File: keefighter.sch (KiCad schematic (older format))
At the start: 49 parts, among them SW0 SW_PUSH, SW1 SW_PUSH, SW10 SW_PUSH, SW11 SW_PUSH, SW12 SW_PUSH, SW13 SW_PUSH, SW14 SW_PUSH, SW15 SW_PUSH, SW16 SW_PUSH, SW17 SW_PUSH, SW2 SW_PUSH, SW3 SW_PUSH, SW4 SW_PUSH, SW5 SW_PUSH, SW6 SW_PUSH, SW7 SW_PUSH, SW8 SW_PUSH, SW9 SW_PUSH, U1 ProMicro

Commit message: Initial Commit
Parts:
- removed D0, D1, D10, D11, D12, D13, D14, D15, D16, D17, D2, D3, D4, D5, D6, D7, D8, D9: 1N4148, Diode_THT:D_DO-35_SOD27_P7.62mm_Horizontal, symbol Diode:1N4148
- removed LED0, LED1, LED10, LED11, LED2, LED3, LED4, LED5, LED6, LED7, LED8, LED9: SK6812MINI, kbd:YS-SK6812MINI-E, symbol keefighter-rescue:SK6812MINI-kbd
- removed SW0, SW12, SW15, SW3, SW6, SW9: SW_PUSH, Button_Switch_THT:SW_PUSH_6mm, symbol keefighter-rescue:SW_PUSH-kbd
- removed SW1, SW10, SW11, SW13, SW14, SW16, SW17, SW2, SW4, SW5, SW7, SW8: SW_PUSH, kbd:CherryMX_Hotswap, symbol keefighter-rescue:SW_PUSH-kbd
- removed U1: ProMicro, pro micro:SPARKFUN_PRO_MICRO, symbol keefighter-rescue:ProMicro-kbd
- added C0, C1, C2, C3: 0.1u, symbol Device:C_Small
- added C4: 10u, symbol Device:C_Small
- added C5, C6: 22p, symbol Device:C_Small
- added C7: 1u, symbol Device:C_Small
- added D0, D1, D10, D11, D12, D13, D14, D15, D16, D17, D18, D19, D2, D20, D21, D22, D23, D24, D25, D26, D27, D28, D29, D3, D30, D31, D32, D33, D34, D4, D5, D6, D7, D8, D9: D, symbol Device:D
- added D35: PRTR5V0U2X, Package_TO_SOT_SMD:SOT-143, symbol Power_Protection:PRTR5V0U2X
- added F0: 500m, symbol Device:Polyfuse_Small
- added J0: AVR-ISP-6, symbol Connector:AVR-ISP-6
- added R0, R1: 10k, symbol Device:R_Small
- added R2, R3: 22, symbol Device:R_Small
- added R4, R5: 5.1k, symbol Device:R_Small
- added SW0, SW1, SW10, SW11, SW12, SW13, SW14, SW15, SW16, SW17, SW18, SW19, SW2, SW20, SW21, SW22, SW23, SW24, SW25, SW26, SW27, SW28, SW29, SW3, SW30, SW31, SW32, SW33, SW34, SW4, SW5, SW6, SW7, SW8, SW9: SW_Push, symbol Switch:SW_Push
- added SW35: SW_Push_Reset, symbol Switch:SW_Push
- added U0: ATmega32U4-AU, Package_QFP:TQFP-44_10x10mm_P0.8mm, symbol MCU_Microchip_ATmega:ATmega32U4-AU
- added USB0: HRO-TYPE-C-31-M-12, symbol Type-C:HRO-TYPE-C-31-M-12
- added X0: XTAL, symbol Device:Crystal_GND24_Small
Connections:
- net labels added: +5V, D+, D-, GND, MISO, MOSI, RESET, SCK, VCC, XTAL1, XTAL2, col10, col11, col12, col6, col7, col8, col9
- net labels removed: din, gnd, vcc
- wire segments 115 -> 180
- no-connect marks 0 -> 10

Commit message: asdfasf
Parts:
- removed SW1, SW33: SW_Push, symbol Switch:SW_Push
- added JOY0, JOY1: COM-09032, XDCR_COM-09032, symbol Joystick:COM-09032
- C0, C1, C2, C3, C4, C5, C6, C7: footprint (none) -> Capacitor_SMD:C_0805_2012Metric_Pad1.18x1.45mm_HandSolder
- D0, D1, D10, D11, D12, D13, D14, D15, D16, D17, D18, D19, D2, D20, D21, D22, D23, D24, D25, D26, D27, D28, D29, D3, D30, D31, D32, D33, D34, D4, D5, D6, D7, D8, D9: footprint (none) -> lib:D3_TH_SMD_v2
- D35: footprint Package_TO_SOT_SMD:SOT-143 -> lib:SOT143B
- F0: footprint (none) -> Fuse:Fuse_1206_3216Metric_Pad1.42x1.75mm_HandSolder
- J0: footprint (none) -> lib:Reset_Pretty-Mask
- R0, R1, R2, R3, R4, R5: footprint (none) -> Resistor_SMD:R_0805_2012Metric_Pad1.20x1.40mm_HandSolder
- USB0: footprint (none) -> lib:HRO-TYPE-C-31-M-12-HandSoldering
- X0: footprint (none) -> Crystal:Crystal_SMD_3225-4Pin_3.2x2.5mm_HandSoldering
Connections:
- net col1: now also JOY0.B1A (SEL+), JOY1.B1A (SEL+)
- net at D1.2 (A): now also JOY0.B2A (SEL-)
- net at D33.2 (A): now also JOY1.B2A (SEL-)
- new net: JOY0.S1 (SHIELD), JOY0.S2 (SHIELD), JOY0.S3 (SHIELD), JOY0.S4 (SHIELD)
- new net: JOY1.S1 (SHIELD), JOY1.S2 (SHIELD), JOY1.S3 (SHIELD), JOY1.S4 (SHIELD)
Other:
- moved on the sheet: C0, C1, C2, C3, C4, C5, C6, C7, D0, D1, D10, D11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

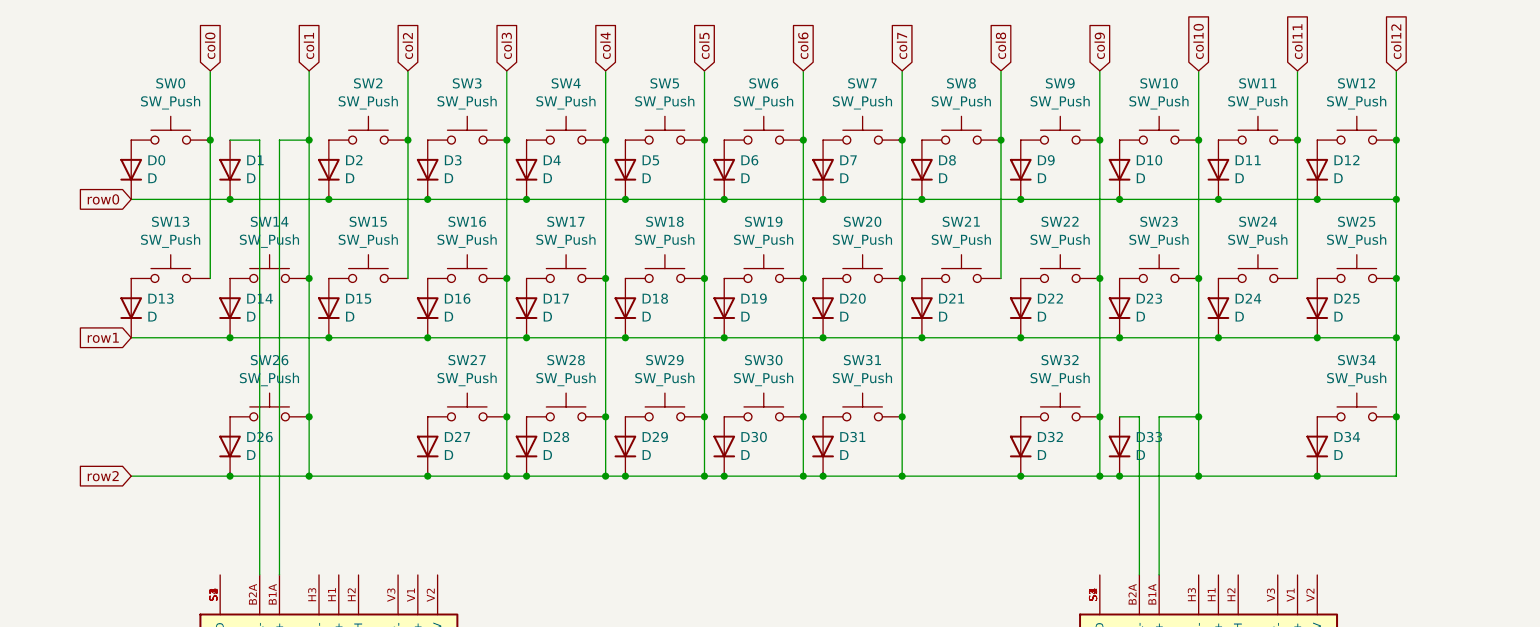
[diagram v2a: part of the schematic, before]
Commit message: Fixed routing issues with matrix
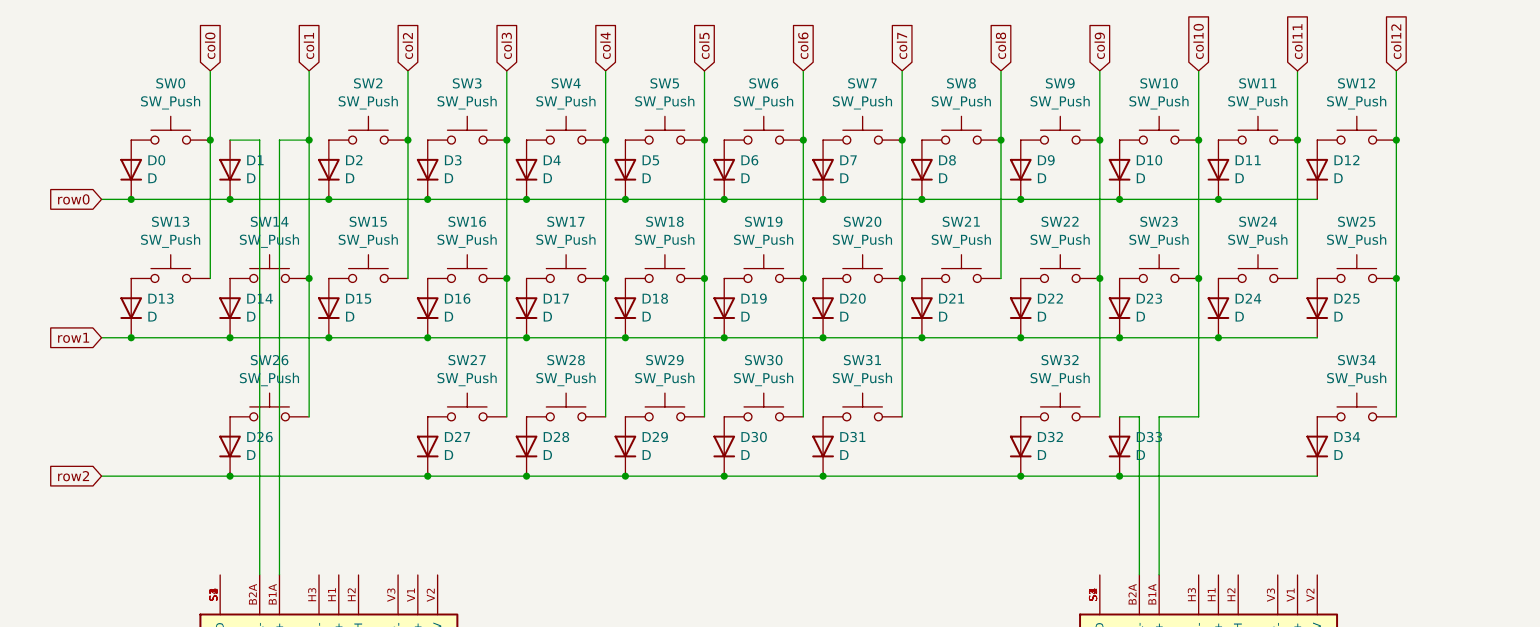
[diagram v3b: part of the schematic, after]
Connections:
- net col1: no longer D0.1 (K), D1.1 (K), D10.1 (K), D11.1 (K), D12.1 (K), D13.1 (K), D14.1 (K), D15.1 (K), D16.1 (K), D17.1 (K), D18.1 (K), D19.1 (K), D2.1 (K), D20.1 (K), D21.1 (K), D22.1 (K), D23.1 (K), D24.1 (K), D25.1 (K), D26.1 (K), D27.1 (K), D28.1 (K), D29.1 (K), D3.1 (K), D30.1 (K), D31.1 (K), D32.1 (K), D33.1 (K), D34.1 (K), D4.1 (K), D5.1 (K), D6.1 (K), D7.1 (K), D8.1 (K), D9.1 (K), JOY1.B1A (SEL+), SW10.2, SW12.2, SW16.2, SW17.2, SW18.2, SW19.2, SW20.2, SW22.2, SW23.2, SW25.2, SW27.2, SW28.2, SW29.2, SW3.2, SW30.2, SW31.2, SW32.2, SW34.2, SW4.2, SW5.2, SW6.2, SW7.2, SW9.2, U0.1 (PE6), U0.18 (PD0), U0.19 (PD1), U0.20 (PD2), U0.21 (PD3), U0.22 (PD5), U0.26 (PD6), U0.28 (PB4), U0.29 (PB5), U0.32 (PC7), U0.8 (PB0)
- new net col10: JOY1.B1A (SEL+), SW10.2, SW23.2, U0.26 (PD6)
- new net col12: SW12.2, SW25.2, SW34.2, U0.1 (PE6)
- new net col3: SW16.2, SW27.2, SW3.2, U0.32 (PC7)
- new net col4: SW17.2, SW28.2, SW4.2, U0.18 (PD0)
- new net col5: SW18.2, SW29.2, SW5.2, U0.19 (PD1)
- new net col6: SW19.2, SW30.2, SW6.2, U0.20 (PD2)
- new net col7: SW20.2, SW31.2, SW7.2, U0.21 (PD3)
- new net col9: SW22.2, SW32.2, SW9.2, U0.22 (PD5)
- new net row0: D0.1 (K), D1.1 (K), D10.1 (K), D11.1 (K), D12.1 (K), D2.1 (K), D3.1 (K), D4.1 (K), D5.1 (K), D6.1 (K), D7.1 (K), D8.1 (K), D9.1 (K), U0.8 (PB0)
- new net row1: D13.1 (K), D14.1 (K), D15.1 (K), D16.1 (K), D17.1 (K), D18.1 (K), D19.1 (K), D20.1 (K), D21.1 (K), D22.1 (K), D23.1 (K), D24.1 (K), D25.1 (K), U0.28 (PB4)
- new net row2: D26.1 (K), D27.1 (K), D28.1 (K), D29.1 (K), D30.1 (K), D31.1 (K), D32.1 (K), D33.1 (K), D34.1 (K), U0.29 (PB5)
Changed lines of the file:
@@
 Text GLabel 10600 1450 2    50   Input ~ 0
 MISO
-Wire Wire Line
-	5550 2900 5950 2900
 $Comp
 L Device:D D32
@@
 	1    0    0    -1
 $EndComp
-Wire Wire Line
-	4550 2900 4950 2900
 $Comp
 L Device:D D31
@@
 	1    0    0    -1
 $EndComp
-Wire Wire Line
-	4050 2900 4450 2900
 $Comp
 L Device:D D30
@@
 	1    0    0    -1
 $EndComp
-Wire Wire Line
-	3550 2900 3950 2900
 $Comp
 L Device:D D29
@@
 	1    0    0    -1
 $EndComp
-Wire Wire Line
-	3050 2900 3450 2900
 $Comp
 L Device:D D28
@@
 	1    0    0    -1
 $EndComp
-Wire Wire Line
-	2550 2900 2950 2900
 $Comp
 L Device:D D27
@@
 	1    0    0    -1
 $EndComp
-Connection ~ 1950 2600
-Wire Wire Line
-	1550 2900 1950 2900
 $Comp
 L Device:D D26
@@
 $EndComp
 Wire Wire Line
-	2450 850  2450 1200
-Wire Wire Line
 	2050 1500 2550 1500
 $Comp
@@
 	0    -1   -1   0
 $EndComp
-Wire Wire Line
-	1950 2600 1950 2900
-Wire Wire Line
-	2950 2600 2950 2900
-Connection ~ 2950 2900
-Wire Wire Line
-	2950 2900 3050 2900
-Wire Wire Line
-	3450 2600 3450 2900
-Connection ~ 3450 2900
-Wire Wire Line
-	3450 2900 3550 2900
-Wire Wire Line
-	3950 2600 3950 2900
-Connection ~ 3950 2900
-Wire Wire Line
-	3950 2900 4050 2900
-Wire Wire Line
-	4450 2600 4450 2900
-Connection ~ 4450 2900
-Wire Wire Line
-	4450 2900 4550 2900
-Wire Wire Line
-	4950 2600 4950 2900
-Wire Wire Line
-	5950 2600 5950 2900
-Wire Wire Line
-	5950 2900 6050 2900
 Connection ~ 4550 1500
 Connection ~ 4550 2200
@@
 Connection ~ 1450 1200
 Wire Wire Line
-	2450 1200 2450 1900
-Connection ~ 2450 1200
-Wire Wire Line
 	2950 1200 2950 1900
 Connection ~ 2950 1200
@@
 Connection ~ 3450 1200
 Wire Wire Line
-	3950 1200 3950 1900
-Connection ~ 3950 1200
-Wire Wire Line
-	4450 1200 4450 1900
-Connection ~ 4450 1200
-Wire Wire Line
 	4950 850  4950 1200
 Wire Wire Line
@@
 	6950 1900 6950 1200
 Wire Wire Line
-	7450 1900 7450 1500
-Wire Wire Line
 	5950 850  5950 1200
 Connection ~ 5950 1200
@@
 	7450 850  7450 1200
 Connection ~ 7450 1200
-Connection ~ 3050 2900
-Connection ~ 3550 2900
-Connection ~ 4050 2900
-Connection ~ 4550 2900
-Wire Wire Line
-	6050 2900 6450 2900
 $Comp
 L Device:D D33
@@
 	0    -1   -1   0
 $EndComp
-Wire Wire Line
-	7050 2900 7450 2900
 $Comp
 L Device:D D34
@@
 $EndComp
 Wire Wire Line
-	7450 2600 7450 2900
-Connection ~ 6050 2900
-Connection ~ 5950 2900
-Wire Wire Line
 	1950 1900 1950 2600
-Connection ~ 1950 1900
 Wire Wire Line
 	2950 1900 2950 2600
 Connection ~ 2950 1900
-Connection ~ 2950 2600
 Wire Wire Line
 	3450 1900 3450 2600
 Connection ~ 3450 1900
-Connection ~ 3450 2600
-Wire Wire Line
-	3950 1900 3950 2600
-Connection ~ 3950 1900
-Connection ~ 3950 2600
 Wire Wire Line
 	4450 1900 4450 2600
-Connection ~ 4450 1900
-Connection ~ 4450 2600
 Wire Wire Line
 	4950 1900 4950 2600
 Connection ~ 4950 1900
-Connection ~ 4950 2600
 Wire Wire Line
 	5950 1900 5950 2600
 Connection ~ 5950 1900
-Connection ~ 5950 2600
 Connection ~ 6450 1900
-Wire Wire Line
-	7450 1900 7450 2200
 Connection ~ 7450 1900
-Connection ~ 7450 2600
-Wire Wire Line
-	7050 1500 7450 1500
-Connection ~ 7050 1500
-Connection ~ 7450 1500
-Wire Wire Line
-	7450 1500 7450 1200
-Wire Wire Line
-	7050 2200 7450 2200
-Connection ~ 7050 2200
-Connection ~ 7450 2200
-Wire Wire Line
-	7450 2200 7450 2600
-Wire Wire Line
-	7050 2900 6450 2900
-Connection ~ 7050 2900
-Connection ~ 6450 2900
-Wire Wire Line
-	5550 2900 4950 2900
-Connection ~ 5550 2900
-Connection ~ 4950 2900
-Wire Wire Line
-	2550 2900 1950 2900
-Connection ~ 2550 2900
-Connection ~ 1950 2900
-Connection ~ 1550 2900
 Wire Wire Line
 	10350 1450 10600 1450
@@
 $EndComp
 Wire Wire Line
-	1950 850  1950 1200
-Connection ~ 1950 1200
-Wire Wire Line
-	1950 1200 1950 1900
-Wire Wire Line
 	1800 1200 1950 1200
 Wire Wire Line
@@
 Wire Wire Line
 	6150 2600 6050 2600
-Connection ~ 6450 2600
-Wire Wire Line
-	6450 2600 6450 2900
 Wire Wire Line
 	1550 1200 1700 1200
@@
 Text GLabel 10350 1750 2    50   Input ~ 0
 col0
-Wire Wire Line
-	1050 2900 1550 2900
-Text GLabel 1050 2900 0    50   Input ~ 0
+Text GLabel 900  2900 0    50   Input ~ 0
 row2
-Text GLabel 1050 2200 0    50   Input ~ 0
+Text GLabel 900  2200 0    50   Input ~ 0
 row1
-Text GLabel 1050 1500 0    50   Input ~ 0
+Text GLabel 900  1500 0    50   Input ~ 0
 row0
+Wire Wire Line
+	2450 1200 2450 1900
+Connection ~ 2450 1200
+Wire Wire Line
+	2450 850  2450 1200
+Connection ~ 1950 1900
+Wire Wire Line
+	1950 1200 1950 1900
+Connection ~ 1950 1200
+Wire Wire Line
+	1950 850  1950 1200
+Wire Wire Line
+	3950 1900 3950 2600
+Connection ~ 4450 1900
+Connection ~ 4450 1200
+Wire Wire Line
+	4450 1200 4450 1900
+Connection ~ 3950 1900
+Connection ~ 3950 1200
+Wire Wire Line
+	3950 1200 3950 1900
+Connection ~ 6050 2900
+Connection ~ 5550 2900
+Connection ~ 4550 2900
+Connection ~ 4050 2900
+Connection ~ 3550 2900
+Connection ~ 3050 2900
+Connection ~ 2550 2900
+Connection ~ 1550 2900
+Wire Wire Line
+	1550 2900 2550 2900
+Wire Wire Line
+	3050 2900 3550 2900
+Wire Wire Line
+	2550 2900 3050 2900
+Wire Wire Line
+	3550 2900 4050 2900
+Wire Wire Line
+	4050 2900 4550 2900
+Wire Wire Line
+	4550 2900 5550 2900
+Wire Wire Line
+	6050 2900 7050 2900
+Wire Wire Line
+	5550 2900 6050 2900
+Wire Wire Line
+	1050 1500 900  1500
+Connection ~ 1050 1500
+Wire Wire Line
+	1050 2200 900  2200
+Connection ~ 1050 2200
+Wire Wire Line
+	900  2900 1550 2900
+Wire Wire Line
+	7450 1200 7450 1900
+Wire Wire Line
+	7450 1900 7450 2600
 $EndSCHEMATC

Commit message: Use components/schematics from flatbox
jfedor2's flatbox will be used as a guide for building the Keefighter
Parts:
- removed C0: 0.1u, Capacitor_SMD:C_0805_2012Metric_Pad1.18x1.45mm_HandSolder, symbol Device:C_Small
- removed D0, D1, D10, D11, D12, D13, D14, D15, D16, D17, D18, D19, D2, D20, D21, D22, D23, D24, D25, D26, D27, D28, D29, D3, D30, D31, D32, D33, D34, D4, D5, D6, D7, D8, D9: D, lib:D3_TH_SMD_v2, symbol Device:D
- removed D35: PRTR5V0U2X, lib:SOT143B, symbol Power_Protection:PRTR5V0U2X
- removed F0: 500m, Fuse:Fuse_1206_3216Metric_Pad1.42x1.75mm_HandSolder, symbol Device:Polyfuse_Small
- removed J0: AVR-ISP-6, lib:Reset_Pretty-Mask, symbol Connector:AVR-ISP-6
- removed JOY0, JOY1: COM-09032, XDCR_COM-09032, symbol Joystick:COM-09032
- removed R0: 10k, Resistor_SMD:R_0805_2012Metric_Pad1.20x1.40mm_HandSolder, symbol Device:R_Small
- removed SW35: SW_Push_Reset, symbol Switch:SW_Push
- removed U0: ATmega32U4-AU, Package_QFP:TQFP-44_10x10mm_P0.8mm, symbol MCU_Microchip_ATmega:ATmega32U4-AU
- removed USB0: HRO-TYPE-C-31-M-12, lib:HRO-TYPE-C-31-M-12-HandSoldering, symbol Type-C:HRO-TYPE-C-31-M-12
- removed X0: XTAL, Crystal:Crystal_SMD_3225-4Pin_3.2x2.5mm_HandSoldering, symbol Device:Crystal_GND24_Small
- added C10, C8: 1u, Capacitor_SMD:C_0402_1005Metric, symbol Device:C_Small
- added C11, C12, C13, C14, C15, C16, C9: 100n, Capacitor_SMD:C_0402_1005Metric, symbol Device:C_Small
- added J6: Conn_02x12_Odd_Even, Connector_PinHeader_2.54mm:PinHeader_2x12_P2.54mm_Vertical, symbol Connector_Generic:Conn_02x12_Odd_Even
- added R6, R7: 5.1k, Resistor_SMD:R_0402_1005Metric, symbol Device:R_Small
- added SW1, SW2, SW3, SW4, SW5, SW6: SW_Push, Button_Switch_THT:SW_PUSH_6mm_H5mm, symbol Switch:SW_Push
- added SW10, SW11, SW12, SW13, SW14, SW15, SW16, SW17, SW18, SW7, SW8, SW9: SW_Push, Kailh:Kailh_socket_PG1350_optional, symbol Switch:SW_Push
- added SW19, SW20: SW_Push, Button_Switch_SMD:SW_SPST_Omron_B3FS-100xP, symbol Switch:SW_Push
- added U1: TLV73333PDBV, Package_TO_SOT_SMD:SOT-23-5, symbol Regulator_Linear:TLV73333PDBV
- added U2: W25Q128JVS, Package_SO:SOIC-8_5.23x5.23mm_P1.27mm, symbol Memory_Flash:W25Q128JVS
- added U3: RP2040, RP2040:RP2040-QFN-56, symbol RP2040:RP2040
- added USB1: HRO-TYPE-C-31-M-12, Type-C:HRO-TYPE-C-31-M-12-Assembly, symbol Type-C:HRO-TYPE-C-31-M-12
- added Y1: Crystal_GND24, Crystal:Crystal_SMD_3225-4Pin_3.2x2.5mm, symbol Device:Crystal_GND24
- C1: value 0.1u -> 1u; footprint Capacitor_SMD:C_0805_2012Metric_Pad1.18x1.45mm_HandSolder -> Capacitor_SMD:C_0402_1005Metric; LCSC (none) -> C52923
- C2, C3: value 0.1u -> 30p; footprint Capacitor_SMD:C_0805_2012Metric_Pad1.18x1.45mm_HandSolder -> Capacitor_SMD:C_0402_1005Metric; LCSC (none) -> C1570
- C4: value 10u -> 1u; footprint Capacitor_SMD:C_0805_2012Metric_Pad1.18x1.45mm_HandSolder -> Capacitor_SMD:C_0402_1005Metric; LCSC (none) -> C52923
- C5, C6: value 22p -> 100n; footprint Capacitor_SMD:C_0805_2012Metric_Pad1.18x1.45mm_HandSolder -> Capacitor_SMD:C_0402_1005Metric; LCSC (none) -> C1525
- C7: value 1u -> 100n; footprint Capacitor_SMD:C_0805_2012Metric_Pad1.18x1.45mm_HandSolder -> Capacitor_SMD:C_0402_1005Metric; LCSC (none) -> C1525
- R1: value 10k -> 1k; footprint Resistor_SMD:R_0805_2012Metric_Pad1.20x1.40mm_HandSolder -> Resistor_SMD:R_0402_1005Metric; LCSC (none) -> C11702
- R2: value 22 -> 10k; footprint Resistor_SMD:R_0805_2012Metric_Pad1.20x1.40mm_HandSolder -> Resistor_SMD:R_0402_1005Metric; LCSC (none) -> C25744
- R3: value 22 -> 27; footprint Resistor_SMD:R_0805_2012Metric_Pad1.20x1.40mm_HandSolder -> Resistor_SMD:R_0402_1005Metric; LCSC (none) -> C138021
- R4: value 5.1k -> 27; footprint Resistor_SMD:R_0805_2012Metric_Pad1.20x1.40mm_HandSolder -> Resistor_SMD:R_0402_1005Metric; LCSC (none) -> C138021
- R5: value 5.1k -> 1k; footprint Resistor_SMD:R_0805_2012Metric_Pad1.20x1.40mm_HandSolder -> Resistor_SMD:R_0402_1005Metric; LCSC (none) -> C11702
- SWL_0: renamed from SW27; value SW_Push -> B_START
- SWL_1: renamed from SW2; value SW_Push -> B_L1
- SWL_10: renamed from SW18; value SW_Push -> B_L8
- SWL_11: renamed from SW13; value SW_Push -> B_DPAD_L
- SWL_12: renamed from SW14; value SW_Push -> B_DPAD_D
- SWL_13: renamed from SW6; value SW_Push -> B_CAPTURE
- SWL_14: renamed from SW28; value SW_Push -> B_L9
- SWL_15: renamed from SW29; value SW_Push -> B_L10
- SWL_2: renamed from SW3; value SW_Push -> B_L2
- SWL_3: renamed from SW4; value SW_Push -> B_L3
- SWL_4: renamed from SW5; value SW_Push -> B_L4
- SWL_5: renamed from SW0; value SW_Push -> B_DPAD_U
- SWL_6: renamed from SW26; value SW_Push -> B_DPAD_R
- SWL_7: renamed from SW15; value SW_Push -> B_L5
- SWL_8: renamed from SW16; value SW_Push -> B_L6
- SWL_9: renamed from SW17; value SW_Push -> B_L7
- SWM_0: renamed from SW30; value SW_Push -> B_JUMP
- SWR_0: renamed from SW11; value SW_Push -> B_SELECT
- SWR_1: renamed from SW10; value SW_Push -> B_R1
- SWR_10: renamed from SW20; value SW_Push -> B_R8
- SWR_11: renamed from SW34; value SW_Push -> B_B
- SWR_12: renamed from SW32; value SW_Push -> B_Y
- SWR_13: renamed from SW19; value SW_Push -> B_HOME
- SWR_14: renamed from SW12; value SW_Push -> B_R9
- SWR_15: renamed from SW31; value SW_Push -> B_R10
- SWR_2: renamed from SW9; value SW_Push -> B_R2
- SWR_3: renamed from SW8; value SW_Push -> B_R3
- SWR_4: renamed from SW7; value SW_Push -> B_R4
- SWR_5: renamed from SW25; value SW_Push -> B_A
- SWR_6: renamed from SW24; value SW_Push -> B_X
- SWR_7: renamed from SW23; value SW_Push -> B_R5
- SWR_8: renamed from SW22; value SW_Push -> B_R6
- SWR_9: renamed from SW21; value SW_Push -> B_R7
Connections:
- net XTAL2 is gone; now on net +1V1: C6.1
- net col0 is gone; now on net GND: SWL_11.2, SWL_5.2
- net col1 is gone; now on net GND: SWL_12.2, SWL_6.2
- net col2 is gone; now on net GND: SWL_1.2, SWL_7.2
- net col3 is gone; now on net GND: SWL_0.2, SWL_2.2, SWL_8.2
- net col4 is gone; now on net GND: SWL_14.2, SWL_3.2, SWL_9.2
- net col5 is gone; now on net GND: SWL_10.2, SWL_15.2, SWL_4.2
- net +5V: now also J6.14 (Pin_14), U1.1 (IN), U1.3 (EN), USB1.11 (VBUS), USB1.2 (VBUS); no longer C2.1, C3.1, C4.1
- net D+: now also R3.1, USB1.6 (DP1), USB1.8 (DP2); no longer R3.2
- net D-: now also R4.1, USB1.5 (DN2), USB1.7 (DN1); no longer R2.1
- net GND: now also C2.1, SWL_13.2, SWM_0.1, SWR_0.1, SWR_1.1, SWR_10.1, SWR_11.1, SWR_12.1, SWR_13.1, SWR_14.1, SWR_15.1, SWR_2.1, SWR_3.1, SWR_4.1, SWR_5.1, SWR_6.1, SWR_7.1, SWR_8.1, SWR_9.1, C10.2, C11.2, C12.2, C13.2, C14.2, C15.2, C16.2, C8.2, C9.2, J6.12 (Pin_12), R6.2, R7.2, SW1.2, SW10.2, SW11.2, SW12.2, SW13.2, SW14.2, SW15.2, SW16.2, SW17.2, SW18.2, SW19.1, SW2.2, SW20.1, SW3.2, SW4.2, SW5.2, SW6.2, SW7.2, SW8.2, SW9.2, U1.2 (GND), U2.4 (GND), U3.19 (TESTEN), U3.57 (GND), USB1.1 (GND), USB1.12 (GND), USB1.13 (SHIELD), Y1.2, Y1.4; no longer C2.2, R1.1, R4.2, R5.1
- net at R1.2: now also SW19.2
- net +1V1: now reaches C7.1
- net +1V1: now also C8.1, U3.23 (DVDD), U3.45 (VREG_VOUT), U3.50 (DVDD)
- net XOUT: now reaches R5.2
- net XOUT: now also U3.21 (XOUT)
- net QSPI_SS: now reaches R2.2
- net QSPI_SS: now also R1.1, U2.1 (~CS), U3.56 (QSPI_SS)
- net B_DPAD_U: now reaches SWL_5.1
- net B_L1: now reaches SWL_1.1
- net B_L1: now also J6.8 (Pin_8)
- net B_L2: now reaches SWL_2.1
- net B_L2: now also J6.6 (Pin_6)
- net B_L3: now reaches SWL_3.1
- net B_L3: now also J6.4 (Pin_4)
- net B_L4: now reaches SWL_4.1
- net B_L4: now also J6.2 (Pin_2)
- net B_CAPTURE: now reaches SWL_13.1
- net B_DPAD_L: now reaches SWL_11.1
- net B_DPAD_D: now reaches SWL_12.1
- net B_L5: now reaches SWL_7.1
- net B_L5: now also J6.1 (Pin_1)
- net B_L6: now reaches SWL_8.1
- net B_L6: now also J6.3 (Pin_3)
- net B_L7: now reaches SWL_9.1
- net B_L7: now also J6.5 (Pin_5)
- net B_L8: now reaches SWL_10.1
- net B_L8: now also J6.7 (Pin_7)
- net B_DPAD_R: now reaches SWL_6.1
- net B_START: now reaches SWL_0.1
- net B_START: now also J6.10 (Pin_10)
- net B_L9: now reaches SWL_14.1
- net B_L9: now also J6.9 (Pin_9)
- net B_L10: now reaches SWL_15.1
- net XTAL1 renamed +3V3
- net +3V3: now also C4.1, R2.1, C10.1, C11.1, C12.1, C13.1, C14.1, C15.1, C16.1, C9.1, U1.5 (OUT), U2.8 (VCC), U3.1 (IOVDD), U3.10 (IOVDD), U3.22 (IOVDD), U3.33 (IOVDD), U3.42 (IOVDD), U3.43 (ADC_AVDD), U3.44 (VREG_IN), U3.48 (USB_VDD), U3.49 (IOVDD)
- net col10 renamed B_R1
- net B_R1: now also J6.18 (Pin_18); no longer SWR_7.2
- net col11 renamed B_RX
- net B_RX: no longer SWR_0.2
- removed net col12: SWR_11.2, SWR_14.2, SWR_5.2
- removed net col6: SWL_13.2, SWM_0.2, SWR_13.2
- removed net col7: SWR_10.2, SWR_15.2, SWR_4.2
- net col8 renamed B_R3
- net B_R3: now also J6.22 (Pin_22); no longer SWR_9.2
- removed net col9: SWR_12.2, SWR_2.2, SWR_8.2
- new net: SW20.2, U3.26 (RUN)
- new net: R4.2, U3.46 (USB_DM)
- new net: R3.2, U3.47 (USB_DP)
- new net: C3.1, R5.1, Y1.3
- new net: R6.1, USB1.10 (CC2)
- new net: R7.1, USB1.4 (CC1)
- new net B_A: SWR_5.2
- new net B_B: SWR_11.2
- new net B_HOME: SWR_13.2
- new net B_JUMP: J6.13 (Pin_13), SWM_0.2
- new net B_R10: SWR_15.2
- new net B_R2: J6.20 (Pin_20), SWR_2.2
- new net B_R4: J6.24 (Pin_24), SWR_4.2
- new net B_R5: J6.23 (Pin_23), SWR_7.2
- new net B_R6: J6.21 (Pin_21), SWR_8.2
- new net B_R7: J6.19 (Pin_19), SWR_9.2
- new net B_R8: J6.17 (Pin_17), SWR_10.2
- new net B_R9: J6.15 (Pin_15), SWR_14.2
- new net B_SELECT: J6.16 (Pin_16), SWR_0.2
- new net B_Y: SWR_12.2
- new net CIRCLE: SW15.1, U3.36 (GPIO24)
- new net CROSS: SW14.1, U3.30 (GPIO19)
- new net DOWN: SW8.1, U3.13 (GPIO10)
- new net L1: SW13.1, U3.41 (GPIO29_ADC3)
- new net L2: SW17.1, U3.40 (GPIO28_ADC2)
- new net LEFT: SW7.1, U3.12 (GPIO9)
- new net OPT1: SW1.1, U3.8 (GPIO6)
- new net OPT2: SW2.1, U3.7 (GPIO5)
- new net OPT3: SW3.1, U3.6 (GPIO4)
- new net OPT4: SW4.1, U3.5 (GPIO3)
- new net OPT5: SW5.1, U3.4 (GPIO2)
- new net OPT6: SW6.1, U3.3 (GPIO1)
- new net QSPI_SCLK: U2.6 (CLK), U3.52 (QSPI_SCLK)
- new net QSPI_SD0: U2.5 (DI(IO0)), U3.53 (QSPI_SD0)
- new net QSPI_SD1: U2.2 (DO(IO1)), U3.55 (QSPI_SD1)
- new net QSPI_SD2: U2.3 (IO2), U3.54 (QSPI_SD2)
- new net QSPI_SD3: U2.7 (IO3), U3.51 (QSPI_SD3)
- new net R1: SW12.1, U3.39 (GPIO27_ADC1)
- new net R2: SW16.1, U3.38 (GPIO26_ADC0)
- new net RIGHT: SW9.1, U3.14 (GPIO11)
- new net SQUARE: SW10.1, U3.29 (GPIO18)
- new net TRIANGLE: SW11.1, U3.37 (GPIO25)
- new net UP: SW18.1, U3.27 (GPIO16)
- new net XIN: C2.2, U3.20 (XIN), Y1.1
- no-connect marks 10 -> 17
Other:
- note added: "Crystal"
- note added: "Flash"
- note added: "Make sure C10 is close to pin 44 of RP2040"
- note added: "Make sure C8 is close to pin 45 of RP2040"
- note added: "Power"
- note added: "USB"
- moved on the sheet: SWL_0, SWL_1, SWL_10, SWL_11, SWL_12, SWL_13, SWL_14, SWL_15, SWL_2, SWL_3, SWL_4, SWL_5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
